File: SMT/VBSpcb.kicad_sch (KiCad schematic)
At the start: 15 parts, among them J1 Video In GND, J2 DB25_Receptacle, J3 Video In Sig, U1 LF356

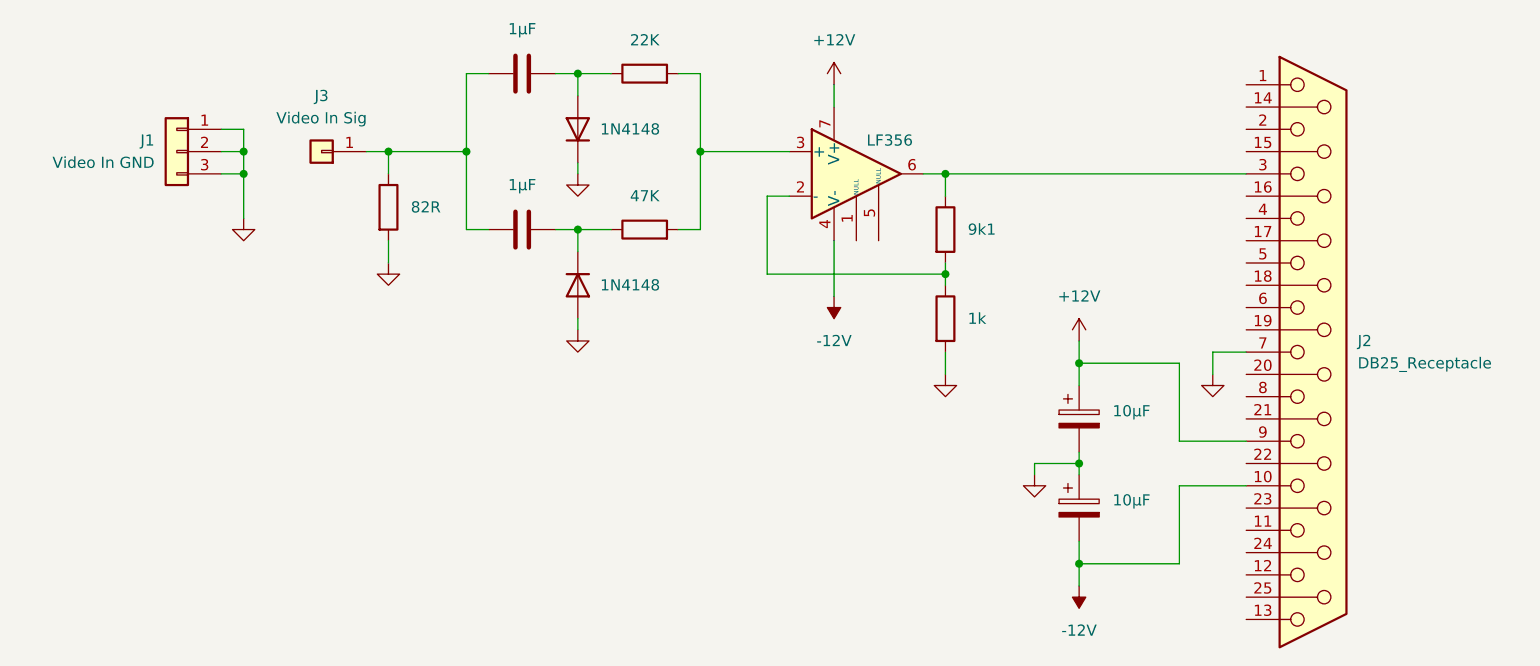
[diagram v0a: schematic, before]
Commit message: Added SMT version and moved THT to it's own folder
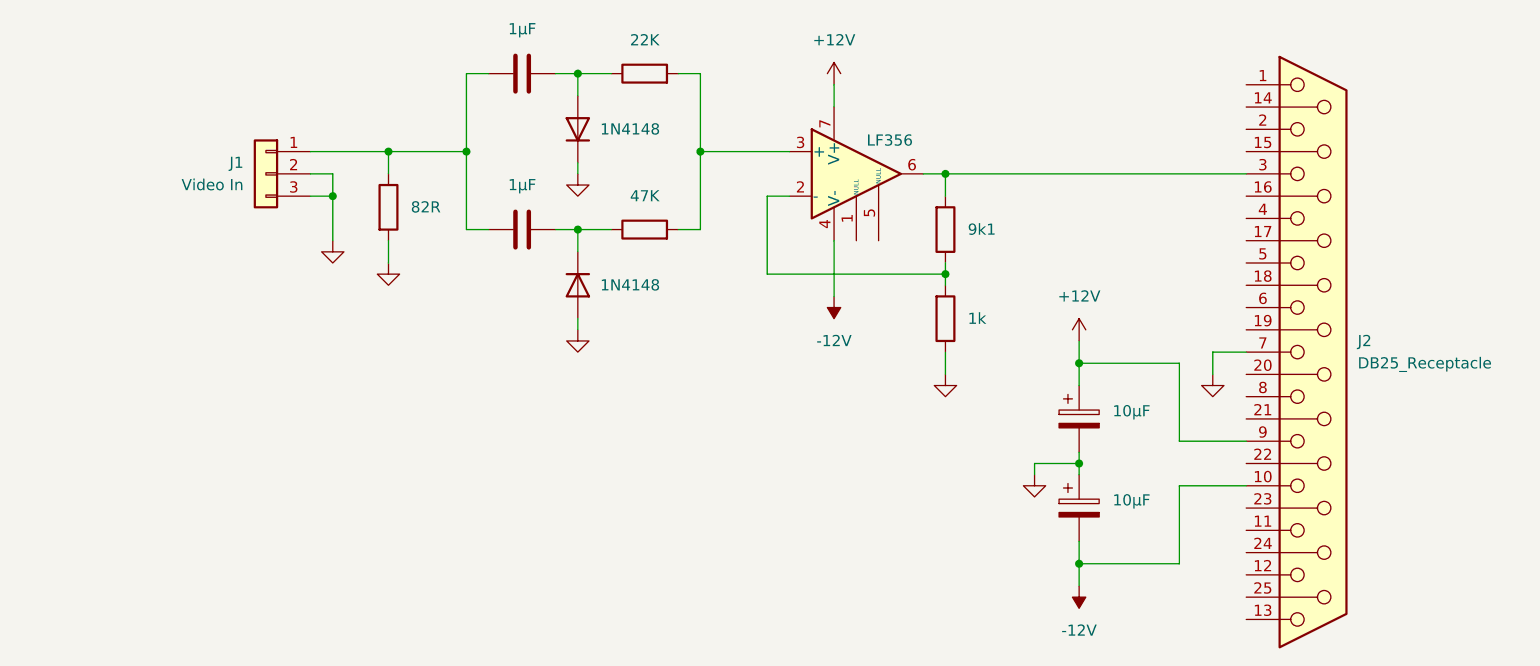
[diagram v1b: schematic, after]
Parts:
- removed J3: Video In Sig, Connector_PinHeader_2.54mm:PinHeader_1x01_P2.54mm_Vertical, symbol Connector_Generic:Conn_01x01
- C1, C2: footprint Capacitor_THT:C_Rect_L7.2mm_W5.5mm_P5.00mm_FKS2_FKP2_MKS2_MKP2 -> Capacitor_SMD:C_1210_3225Metric_Pad1.33x2.70mm_HandSolder
- C3, C4: footprint Capacitor_THT:CP_Radial_D5.0mm_P2.00mm -> Capacitor_SMD:CP_Elec_5x5.4
- D1, D2: footprint Diode_THT:D_DO-35_SOD27_P7.62mm_Horizontal -> Diode_SMD:D_SOD-323_HandSoldering
- J1: value Video In GND -> Video In
- R1, R2, R3, R4, R5: footprint Resistor_THT:R_Axial_DIN0207_L6.3mm_D2.5mm_P7.62mm_Horizontal -> Resistor_SMD:R_1206_3216Metric_Pad1.30x1.75mm_HandSolder
- U1: footprint Package_DIP:DIP-8_W7.62mm_Socket -> Package_SO:SO-8_3.9x4.9mm_P1.27mm
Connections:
- net GND: now also R5.1; no longer J1.1 (Pin_1), R5.2
- net at C2.1, R1.1: now also C1.2, J1.1 (Pin_1); no longer C1.1
- net at D1.2 (A), R2.1: now also C1.1; no longer C1.2
- net at J2.3, U1.6: now also R4.2; no longer R4.1
- new net: R4.1, R5.2, U1.2 (-)
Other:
- moved on the sheet: J1
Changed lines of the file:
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@@
   (junction (at 63.5 80.01) (diameter 0) (color 0 0 0 0)
   )
-  (junction (at 46.99 82.55) (diameter 0) (color 0 0 0 0)
+  (junction (at 57.15 85.09) (diameter 0) (color 0 0 0 0)
   )
   (junction (at 72.39 80.01) (diameter 0) (color 0 0 0 0)
@@
   (junction (at 127 82.55) (diameter 0) (color 0 0 0 0)
   )
-  (junction (at 46.99 80.01) (diameter 0) (color 0 0 0 0)
-  )
   (wire (pts (xy 99.06 71.12) (xy 99.06 80.01))
     (stroke (width 0) (type default))
@@
     (stroke (width 0) (type default))
   )
-  (wire (pts (xy 60.96 80.01) (xy 63.5 80.01))
+  (wire (pts (xy 54.61 80.01) (xy 63.5 80.01))
     (stroke (width 0) (type default))
   )
@@
     (stroke (width 0) (type default))
   )
-  (wire (pts (xy 44.45 77.47) (xy 46.99 77.47))
-    (stroke (width 0) (type default))
-  )
   (wire (pts (xy 142.24 115.57) (xy 142.24 116.84))
     (stroke (width 0) (type default))
   )
-  (wire (pts (xy 44.45 82.55) (xy 46.99 82.55))
+  (wire (pts (xy 54.61 85.09) (xy 57.15 85.09))
     (stroke (width 0) (type default))
   )
@@
     (stroke (width 0) (type default))
   )
-  (wire (pts (xy 46.99 82.55) (xy 46.99 87.63))
+  (wire (pts (xy 57.15 85.09) (xy 57.15 90.17))
     (stroke (width 0) (type default))
   )
@@
     (stroke (width 0) (type default))
   )
-  (wire (pts (xy 46.99 77.47) (xy 46.99 80.01))
-    (stroke (width 0) (type default))
-  )
   (wire (pts (xy 85.09 81.28) (xy 85.09 82.55))
     (stroke (width 0) (type default))
@@
     (stroke (width 0) (type default))
   )
-  (wire (pts (xy 46.99 80.01) (xy 46.99 82.55))
+  (wire (pts (xy 57.15 82.55) (xy 57.15 85.09))
     (stroke (width 0) (type default))
   )
@@
     (stroke (width 0) (type default))
   )
-  (wire (pts (xy 44.45 80.01) (xy 46.99 80.01))
+  (wire (pts (xy 54.61 82.55) (xy 57.15 82.55))
     (stroke (width 0) (type default))
   )
@@
       (effects (font (size 1.27 1.27)) (justify left))
     )
-    (property "Footprint" "Diode_THT:D_DO-35_SOD27_P7.62mm_Horizontal" (at 85.09 95.25 0)
+    (property "Footprint" "Diode_SMD:D_SOD-323_HandSoldering" (at 85.09 95.25 0)
       (effects (font (size 1.27 1.27)) hide)
     )
@@
       (effects (font (size 1.27 1.27)) (justify left))
     )
-    (property "Footprint" "Capacitor_THT:CP_Radial_D5.0mm_P2.00mm" (at 143.2052 114.3 0)
+    (property "Footprint" "Capacitor_SMD:CP_Elec_5x5.4" (at 143.2052 114.3 0)
       (effects (font (size 1.27 1.27)) hide)
     )
@@
     )
   )
-  (symbol (lib_id "Device:C") (at 78.74 71.12 90) (unit 1)
-    (in_bom yes) (on_board yes) (dnp no) (fields_autoplaced)
+  (symbol (lib_id "Device:C") (at 78.74 71.12 270) (mirror x) (unit 1)
+    (in_bom yes) (on_board yes) (dnp no)
     (property "Reference" "C1" (at 78.74 63.5 90)
       (effects (font (size 1.27 1.27)) hide)
@@
       (effects (font (size 1.27 1.27)))
     )
-    (property "Footprint" "Capacitor_THT:C_Rect_L7.2mm_W5.5mm_P5.00mm_FKS2_FKP2_MKS2_MKP2" (at 82.55 70.1548 0)
+    (property "Footprint" "Capacitor_SMD:C_1210_3225Metric_Pad1.33x2.70mm_HandSolder" (at 74.93 70.1548 0)
       (effects (font (size 1.27 1.27)) hide)
     )
@@
     )
   )
-  (symbol (lib_id "Device:R") (at 127 99.06 0) (unit 1)
-    (in_bom yes) (on_board yes) (dnp no) (fields_autoplaced)
-    (property "Reference" "R5" (at 129.54 97.79 0)
+  (symbol (lib_id "Device:R") (at 127 99.06 0) (mirror x) (unit 1)
+    (in_bom yes) (on_board yes) (dnp no)
+    (property "Reference" "R5" (at 129.54 100.33 0)
       (effects (font (size 1.27 1.27)) (justify left) hide)
     )
@@
       (effects (font (size 1.27 1.27)) (justify left))
     )
-    (property "Footprint" "Resistor_THT:R_Axial_DIN0207_L6.3mm_D2.5mm_P7.62mm_Horizontal" (at 125.222 99.06 90)
+    (property "Footprint" "Resistor_SMD:R_1206_3216Metric_Pad1.30x1.75mm_HandSolder" (at 125.222 99.06 90)
       (effects (font (size 1.27 1.27)) hide)
     )
@@
       (effects (font (size 1.27 1.27)) (justify right))
     )
-    (property "Footprint" "Diode_THT:D_DO-35_SOD27_P7.62mm_Horizontal" (at 85.09 77.47 0)
+    (property "Footprint" "Diode_SMD:D_SOD-323_HandSoldering" (at 85.09 77.47 0)
       (effects (font (size 1.27 1.27)) hide)
     )
@@
       (effects (font (size 1.27 1.27)))
     )
-    (property "Footprint" "Capacitor_THT:C_Rect_L7.2mm_W5.5mm_P5.00mm_FKS2_FKP2_MKS2_MKP2" (at 82.55 87.9348 0)
+    (property "Footprint" "Capacitor_SMD:C_1210_3225Metric_Pad1.33x2.70mm_HandSolder" (at 82.55 87.9348 0)
       (effects (font (size 1.27 1.27)) hide)
     )
@@
       (effects (font (size 1.27 1.27)) (justify left))
     )
-    (property "Footprint" "Capacitor_THT:CP_Radial_D5.0mm_P2.00mm" (at 143.2052 124.46 0)
+    (property "Footprint" "Capacitor_SMD:CP_Elec_5x5.4" (at 143.2052 124.46 0)
       (effects (font (size 1.27 1.27)) hide)
     )
@@
     )
   )
-  (symbol (lib_id "power:GND") (at 46.99 87.63 0) (unit 1)
-    (in_bom yes) (on_board yes) (dnp no) (fields_autoplaced)
-    (property "Reference" "#PWR01" (at 46.99 93.98 0)
-      (effects (font (size 1.27 1.27)) hide)
-    )
-    (property "Value" "GND" (at 46.99 92.71 0)
-      (effects (font (size 1.27 1.27)) hide)
-    )
-    (property "Footprint" "" (at 46.99 87.63 0)
-      (effects (font (size 1.27 1.27)) hide)
-    )
-    (property "Datasheet" "" (at 46.99 87.63 0)
+  (symbol (lib_id "power:GND") (at 57.15 90.17 0) (unit 1)
+    (in_bom yes) (on_board yes) (dnp no) (fields_autoplaced)
+    (property "Reference" "#PWR01" (at 57.15 96.52 0)
+      (effects (font (size 1.27 1.27)) hide)
+    )
+    (property "Value" "GND" (at 57.15 95.25 0)
+      (effects (font (size 1.27 1.27)) hide)
+    )
+    (property "Footprint" "" (at 57.15 90.17 0)
+      (effects (font (size 1.27 1.27)) hide)
+    )
+    (property "Datasheet" "" (at 57.15 90.17 0)
       (effects (font (size 1.27 1.27)) hide)
     )
@@
     )
   )
-  (symbol (lib_id "Connector_Generic:Conn_01x01") (at 55.88 80.01 180) (unit 1)
-    (in_bom yes) (on_board yes) (dnp no) (fields_autoplaced)
-    (property "Reference" "J3" (at 55.88 73.66 0)
-      (effects (font (size 1.27 1.27)))
-    )
-    (property "Value" "Video In Sig" (at 55.88 76.2 0)
-      (effects (font (size 1.27 1.27)))
-    )
-    (property "Footprint" "Connector_PinHeader_2.54mm:PinHeader_1x01_P2.54mm_Vertical" (at 55.88 80.01 0)
-      (effects (font (size 1.27 1.27)) hide)
-    )
-    (property "Datasheet" "~" (at 55.88 80.01 0)
-      (effects (font (size 1.27 1.27)) hide)
-    )
-    (pin "1")
-    (instances
-      (project "VBSpcb"
-        (path "/1a8ad53d-58ba-415b-ae19-54d4ebc887f3"
-          (reference "J3") (unit 1)
-        )
-      )
-    )
-  )
   (symbol (lib_id "power:GND") (at 85.09 100.33 0) (unit 1)
     (in_bom yes) (on_board yes) (dnp no) (fields_autoplaced)
@@
       (effects (font (size 1.27 1.27)))
     )
-    (property "Footprint" "Resistor_THT:R_Axial_DIN0207_L6.3mm_D2.5mm_P7.62mm_Horizontal" (at 92.71 72.898 90)
+    (property "Footprint" "Resistor_SMD:R_1206_3216Metric_Pad1.30x1.75mm_HandSolder" (at 92.71 72.898 90)
       (effects (font (size 1.27 1.27)) hide)
     )
@@
       (effects (font (size 1.27 1.27)))
     )
-    (property "Footprint" "Resistor_THT:R_Axial_DIN0207_L6.3mm_D2.5mm_P7.62mm_Horizontal" (at 92.71 90.678 90)
+    (property "Footprint" "Resistor_SMD:R_1206_3216Metric_Pad1.30x1.75mm_HandSolder" (at 92.71 90.678 90)
       (effects (font (size 1.27 1.27)) hide)
     )
@@
     )
   )
-  (symbol (lib_id "Connector_Generic:Conn_01x03") (at 39.37 80.01 0) (mirror y) (unit 1)
+  (symbol (lib_id "Connector_Generic:Conn_01x03") (at 49.53 82.55 0) (mirror y) (unit 1)
     (in_bom yes) (on_board yes) (dnp no)
-    (property "Reference" "J1" (at 36.83 78.74 0)
-      (effects (font (size 1.27 1.27)) (justify left))
-    )
-    (property "Value" "Video In GND" (at 36.83 81.28 0)
-      (effects (font (size 1.27 1.27)) (justify left))
-    )
-    (property "Footprint" "Connector_PinHeader_2.54mm:PinHeader_1x03_P2.54mm_Vertical" (at 39.37 80.01 0)
-      (effects (font (size 1.27 1.27)) hide)
-    )
-    (property "Datasheet" "~" (at 39.37 80.01 0)
+    (property "Reference" "J1" (at 46.99 81.28 0)
+      (effects (font (size 1.27 1.27)) (justify left))
+    )
+    (property "Value" "Video In" (at 46.99 83.82 0)
+      (effects (font (size 1.27 1.27)) (justify left))
+    )
+    (property "Footprint" "Connector_PinHeader_2.54mm:PinHeader_1x03_P2.54mm_Vertical" (at 49.53 82.55 0)
+      (effects (font (size 1.27 1.27)) hide)
+    )
+    (property "Datasheet" "~" (at 49.53 82.55 0)
       (effects (font (size 1.27 1.27)) hide)
     )
@@
       (effects (font (size 1.27 1.27)))
     )
-    (property "Footprint" "Package_DIP:DIP-8_W7.62mm_Socket" (at 118.11 81.28 0)
+    (property "Footprint" "Package_SO:SO-8_3.9x4.9mm_P1.27mm" (at 118.11 81.28 0)
       (effects (font (size 1.27 1.27)) hide)
     )
@@
     )
   )
-  (symbol (lib_id "Device:R") (at 127 88.9 0) (unit 1)
-    (in_bom yes) (on_board yes) (dnp no) (fields_autoplaced)
-    (property "Reference" "R4" (at 129.54 87.63 0)
+  (symbol (lib_id "Device:R") (at 127 88.9 0) (mirror x) (unit 1)
+    (in_bom yes) (on_board yes) (dnp no)
+    (property "Reference" "R4" (at 129.54 90.17 0)
       (effects (font (size 1.27 1.27)) (justify left) hide)
     )
@@
       (effects (font (size 1.27 1.27)) (justify left))
     )
-    (property "Footprint" "Resistor_THT:R_Axial_DIN0207_L6.3mm_D2.5mm_P7.62mm_Horizontal" (at 125.222 88.9 90)
+    (property "Footprint" "Resistor_SMD:R_1206_3216Metric_Pad1.30x1.75mm_HandSolder" (at 125.222 88.9 90)
       (effects (font (size 1.27 1.27)) hide)
     )
@@
       (effects (font (size 1.27 1.27)) (justify left))
     )
-    (property "Footprint" "Resistor_THT:R_Axial_DIN0207_L6.3mm_D2.5mm_P7.62mm_Horizontal" (at 61.722 86.36 90)
-      (effects (font (size 1.27 1.27)) hide)
-    )
+    (property "Footprint" "Resistor_SMD:R_1206_3216Metric_Pad1.30x1.75mm_HandSolder" (at 61.722 86.36 90)
+      (effects (font (size 1.27 1.27)) hide)
+    )
